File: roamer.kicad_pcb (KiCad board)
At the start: 2 copper layers, 103 parts, among them J1 Conn_Coaxial_Small, J2 S2B-PH-K-SLFSN, J3 Conn_02x05_Odd_Even, J4 Conn_Coaxial_Small, J8 MEM2075-00-140-01-A, Q3 DMP2070UQ-7, SW1 KMR2, U1 2MB Flash, U2 AP2112K-3.3, U3 MCP73831-2-OT, U4 RFM95W-915S2, U5 RFM69W, U7 BME688, U8 INA260, X2 32.768 kHz, X3 microUSB 2.0 B

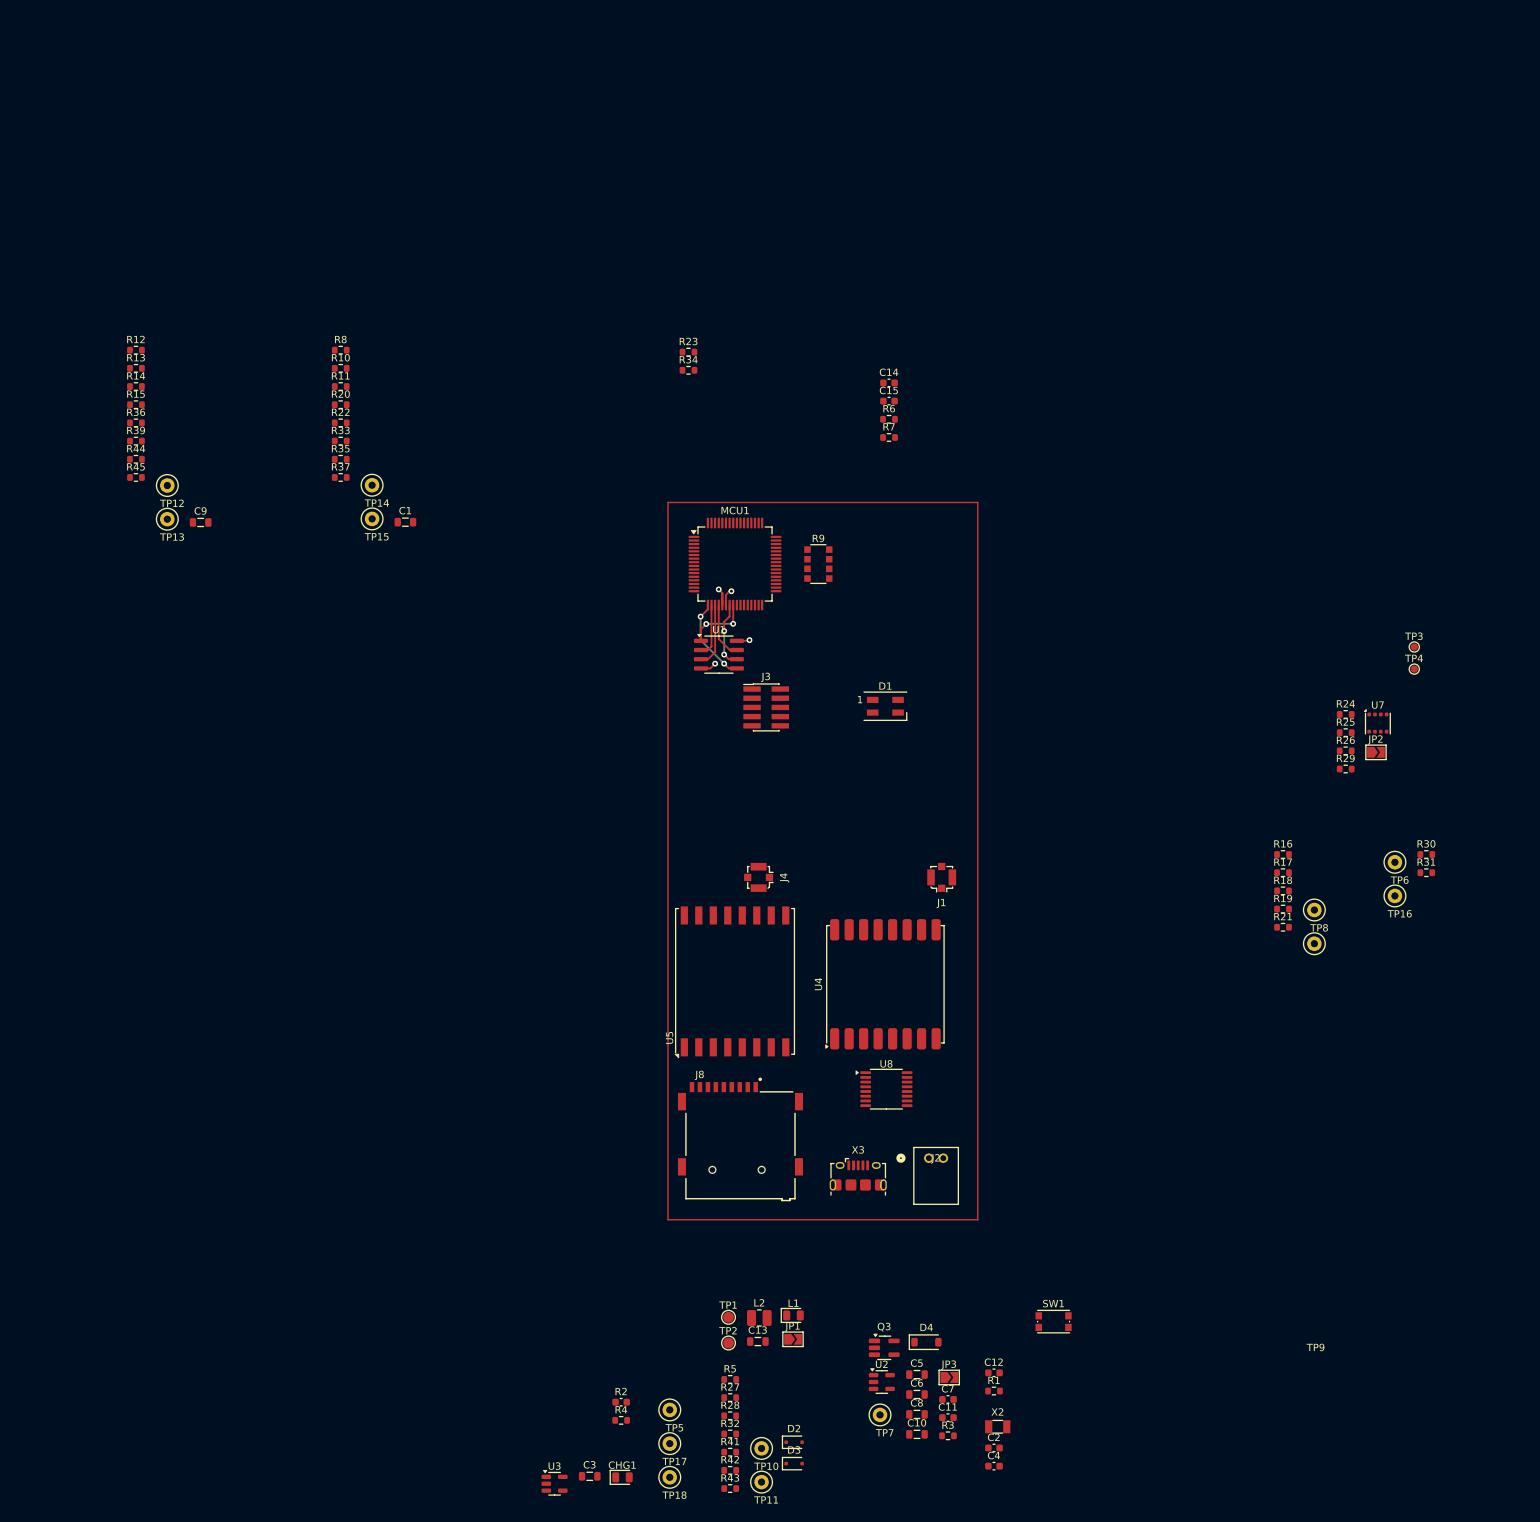
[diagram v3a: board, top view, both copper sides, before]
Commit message: Adding 5V boost
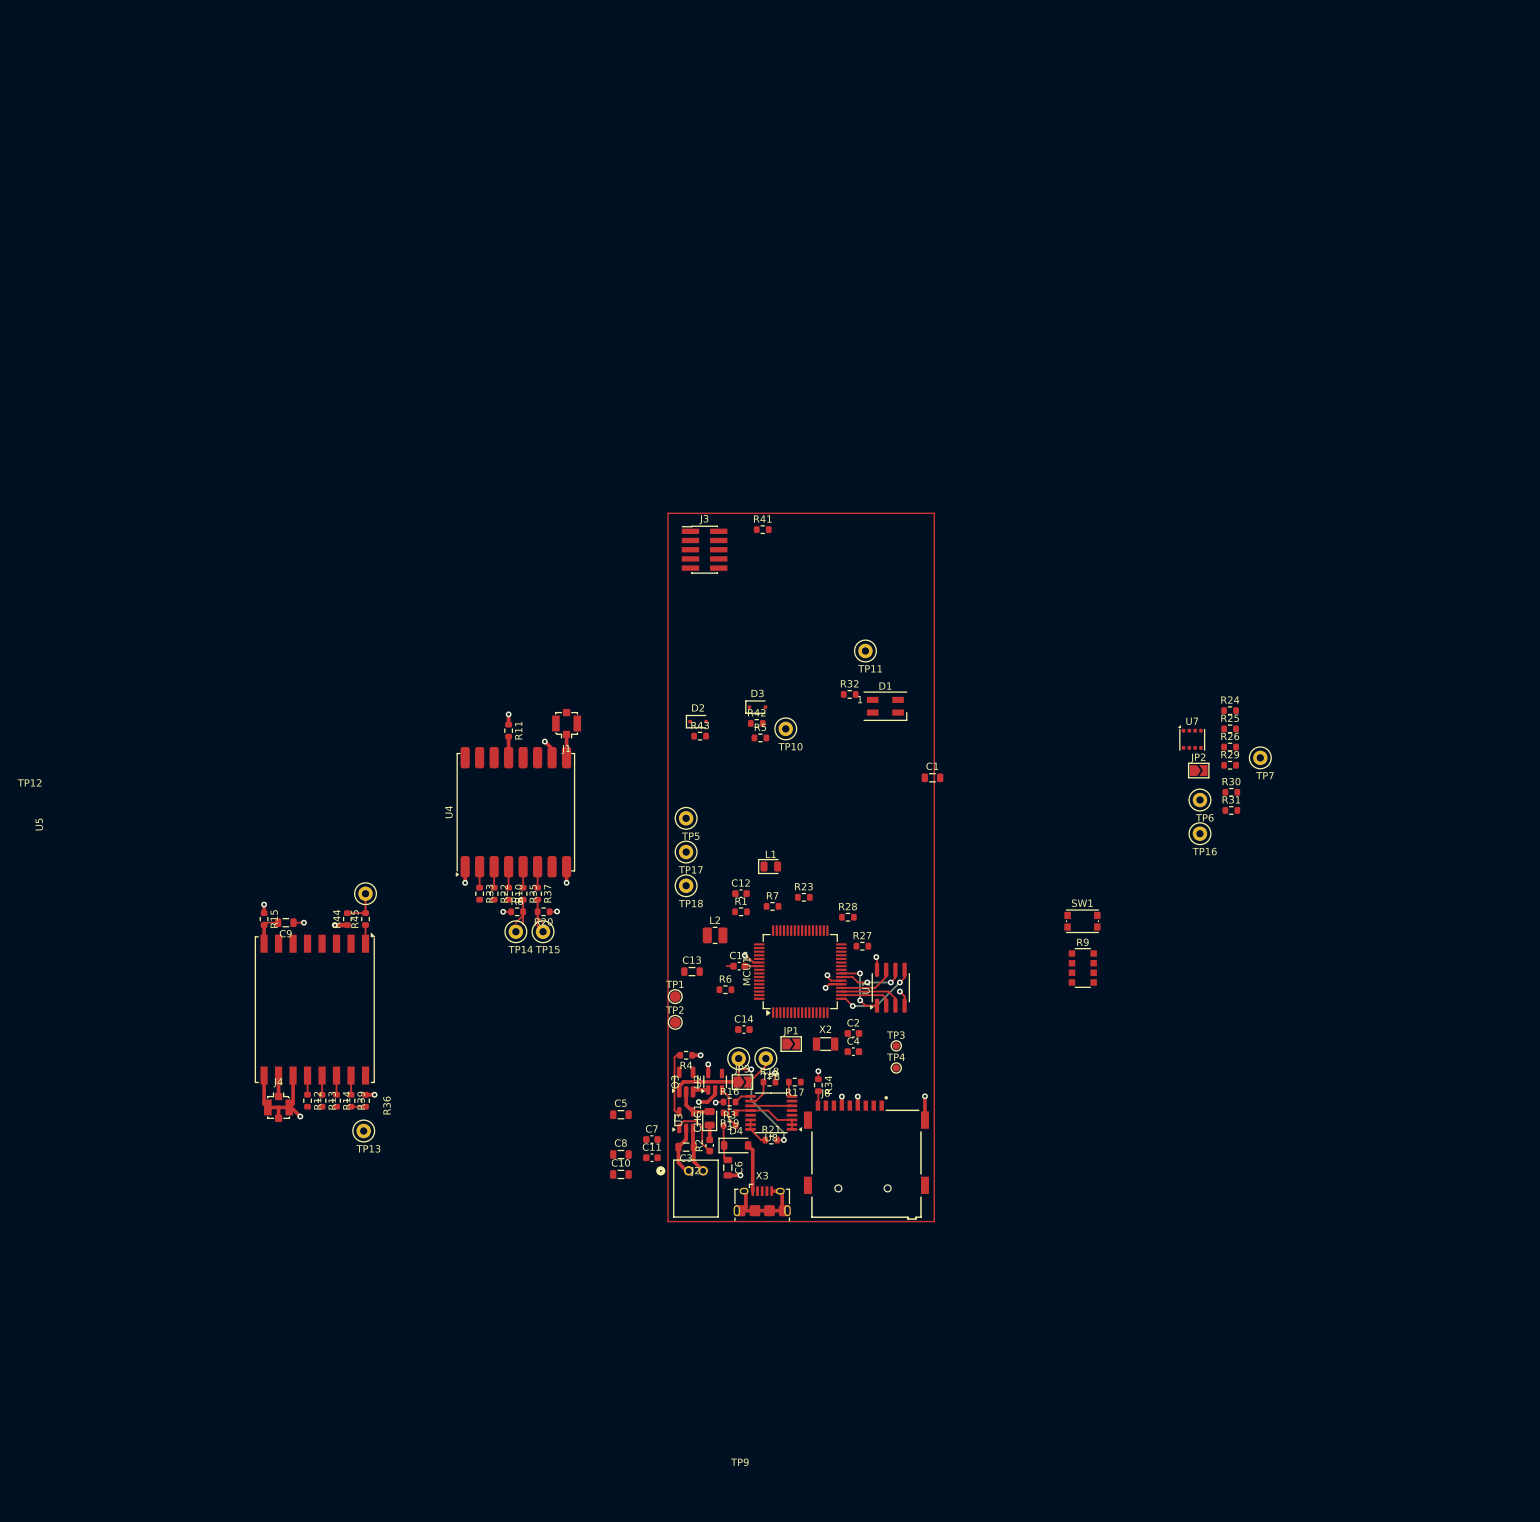
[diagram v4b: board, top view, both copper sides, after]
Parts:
- moved R41 127.4 mm to (204.6, 104.5)
- moved TP11 115.6 mm to (218.8, 121.2)
- moved R12 106.3 mm to (141.8, 183.3), turned to -90 degrees
- moved TP7 104.8 mm to (273.2, 136.0)
- moved D3 104.5 mm to (203.8, 129.0)
- moved R13 104.3 mm to (143.8, 183.3), turned to -90 degrees
- moved R43 103.9 mm to (195.9, 133.0)
- moved R32 103.4 mm to (216.6, 127.2)
- moved R42 103.2 mm to (203.8, 131.2)
- moved R14 102.4 mm to (145.8, 183.3), turned to -90 degrees
- moved D2 100.3 mm to (195.7, 131.0)
- moved R34 100.3 mm to (212.2, 181.2), turned to -90 degrees
- moved TP10 99.4 mm to (207.8, 132.0)
- moved R36 98.8 mm to (149.8, 183.3), turned to -90 degrees
- moved R39 95.8 mm to (147.8, 183.3), turned to -90 degrees
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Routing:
- net GND: track 4.59 -> 68.8 mm, vias 2 -> 13
- net /Power - Management/IN-: track 0.00 -> 26.7 mm, vias 0 -> 2
- net +3V3: track 5.91 -> 18.4 mm, vias 2 -> 12
- net VBUS: track 0.00 -> 12.0 mm
- net +BATT: track 0.00 -> 11.6 mm
- net Net-(U8-VBUS): track 0.00 -> 9.76 mm
- net Net-(U3-PROG): track 0.00 -> 8.94 mm
- net Net-(U3-STAT): track 0.00 -> 7.88 mm
- net Net-(D4-K): track 0.00 -> 7.38 mm
- net Net-(U2-EN): track 0.00 -> 5.69 mm
- net /Comms - LoRa 433/~{RESET_LORA_433}: track 0.00 -> 5.18 mm
- net Net-(U5-3.3V): track 0.00 -> 4.90 mm
- net /Comms - LoRa 900/CS_LORA_900: track 0.00 -> 4.76 mm
- net /Comms - LoRa 900/~{RESET_LORA_900}: track 0.00 -> 4.74 mm
- net Net-(R21-Pad1): track 0.00 -> 3.95 mm
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- added copper zone on In2.Cu, net +3V3
- added copper zone on In1.Cu, net GND
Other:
- copper layers 2 -> 4

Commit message: Working on layout
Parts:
- added C16: 10uF, Inductor_SMD:L_0805_2012Metric, F.Cu at (195.5, 116.2)
- added C17: 10uF, Inductor_SMD:L_0805_2012Metric, F.Cu at (195.5, 122.8)
- added C18: 1uF, Capacitor_SMD:C_0603_1608Metric, F.Cu at (192.6, 120.8)
- added R38: 100K, Resistor_SMD:R_0805_2012Metric, F.Cu at (192.6, 117.2)
- added U6: AP3602AKTR-G1, footprints:SOT-23-6_DIO, F.Cu at (195.5, 119.5)
- J2: value S2B-PH-K-SLFSN -> JSTPH; footprint footprints:CONN_S2B-PH-K-S_JST -> Connector_JST:JST_PH_S2B-PH-SM4-TB_1x02-1MP_P2.00mm_Horizontal
- Q3: footprint Package_TO_SOT_SMD:SOT-23-5_HandSoldering -> Package_TO_SOT_SMD:TSOT-23
- moved TP13 110.1 mm to (246.0, 134.5), turned to 90 degrees
- moved J4 92.2 mm to (223.5, 150.5), turned to -90 degrees
- moved R12 88.8 mm to (222.6, 146.5), turned to 0 degrees
- moved R13 87.9 mm to (222.6, 144.5), turned to 0 degrees
- moved R14 87.0 mm to (222.6, 142.5), turned to 0 degrees
- moved R39 86.2 mm to (222.6, 140.5), turned to 0 degrees
- moved R36 85.5 mm to (222.6, 138.5), turned to 0 degrees
- moved U5 71.8 mm to (210.0, 145.5), turned to 0 degrees
- moved R15 62.0 mm to (197.5, 152.5), turned to 0 degrees
- moved C9 60.0 mm to (198.0, 149.5), turned to -90 degrees
- moved U7 58.8 mm to (210.0, 157.0)
- moved R44 53.1 mm to (197.5, 141.0), turned to 180 degrees
- moved TP17 52.9 mm to (143.2, 133.9)
- moved TP18 52.9 mm to (143.2, 138.6)
- moved TP5 52.9 mm to (143.2, 129.2)
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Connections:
- SW1 pad 2: GND -> /MCU/~{RESET}
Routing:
- net GND: track 68.8 -> 28.8 mm, vias 13 -> 7
- net /Power - Management/IN-: track 26.7 -> 2.28 mm, vias 2 -> 0
- net VBUS: track 12.0 -> 0.00 mm
- net /MCU - Memory/QSPI.DATA0: track 11.9 -> 0.00 mm, vias 2 -> 0
- net /MCU - Memory/QSPI.SCK: track 9.16 -> 0.00 mm, vias 2 -> 0
- net /MCU - Memory/QSPI.CS: track 8.95 -> 0.00 mm, vias 2 -> 0
- net Net-(U3-PROG): track 8.94 -> 0.00 mm
- net /MCU - Memory/QSPI.DATA2: track 8.85 -> 0.00 mm
- net +3V3: track 18.4 -> 10.3 mm, vias 12 -> 6
- net Net-(U3-STAT): track 7.88 -> 0.00 mm
- net /MCU - Memory/QSPI.DATA3: track 7.81 -> 0.00 mm
- net Net-(D4-K): track 7.38 -> 0.00 mm
- net /MCU - Memory/QSPI.DATA1: track 7.37 -> 0.00 mm
- net Net-(U2-EN): track 5.69 -> 0.00 mm
- net Net-(U6-C+): track 0.00 -> 4.93 mm
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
